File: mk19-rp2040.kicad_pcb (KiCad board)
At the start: 2 copper layers, 130 x 102 mm, 145 parts, among them J1 USB_C_Receptacle_USB2.0, J10 Conn_01x02, J11 Conn_01x03_Socket, J12 USB_C_Receptacle_USB2.0, J13 USB_C_Receptacle_USB2.0, J2 Conn_01x03_Socket, J3 Conn_01x02_Socket, J4 Conn_01x06_Socket, J5 Conn_01x02, J7 Conn_01x02_Socket, J8 Conn_01x02_Socket, J9 Conn_01x02_Socket, T1 Conn_01x01_Socket, T10 Conn_01x01_Socket, T11 Conn_01x01_Socket, T12 Conn_01x01_Socket, T13 Conn_01x01_Socket, T14 Conn_01x01_Socket, T15 Conn_01x01_Socket, T2 Conn_01x01_Socket, T3 Conn_01x01_Socket, T5 Conn_01x01_Socket, T6 Conn_01x01_Socket, T7 Conn_01x01_Socket, T9 Conn_01x01_Socket, U1 RP2040, U10 1N4148W_C81598, U11 1N4148W_C81598, U12 1N4148W_C81598, U13 1N4148W_C81598, U14 1N4148W_C81598, U15 1N4148W_C81598, U16 W25Q128JVSIQTR, U3 XC6210B332MR-G, U6 8_01A0_008200, U7 8_01A0_008200, U9 1N4148W_C81598, Y1 Crystal_GND24

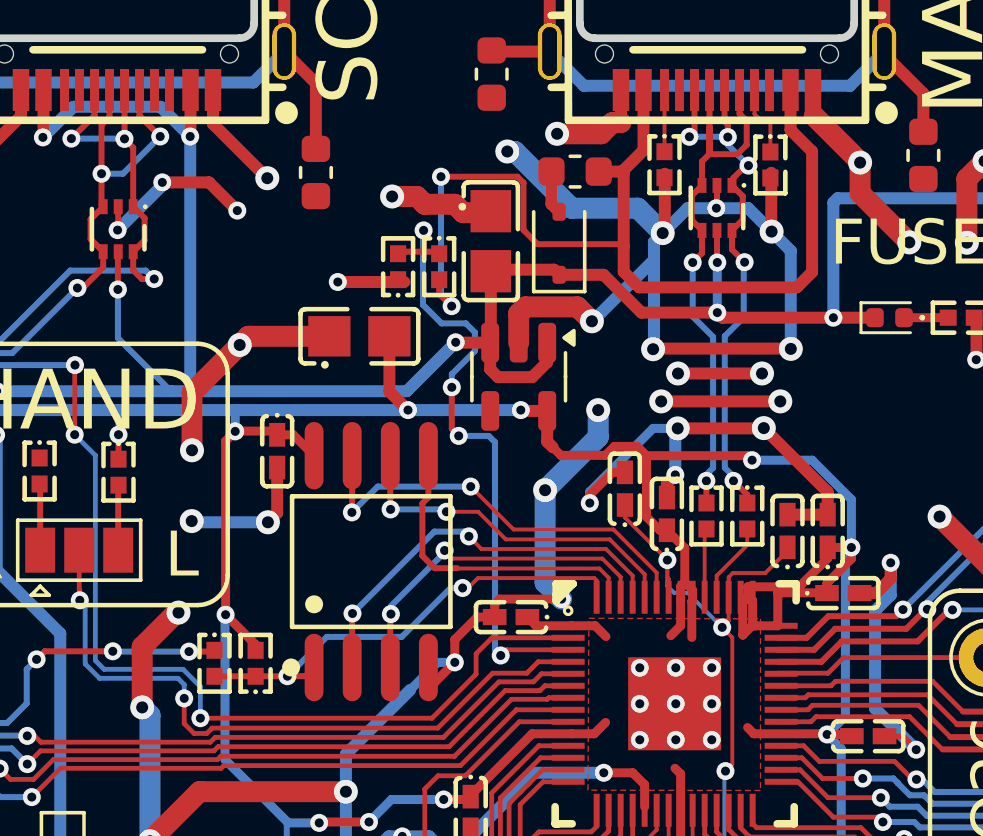
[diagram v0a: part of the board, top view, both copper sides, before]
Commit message: reworking the voltage regulator capacitors
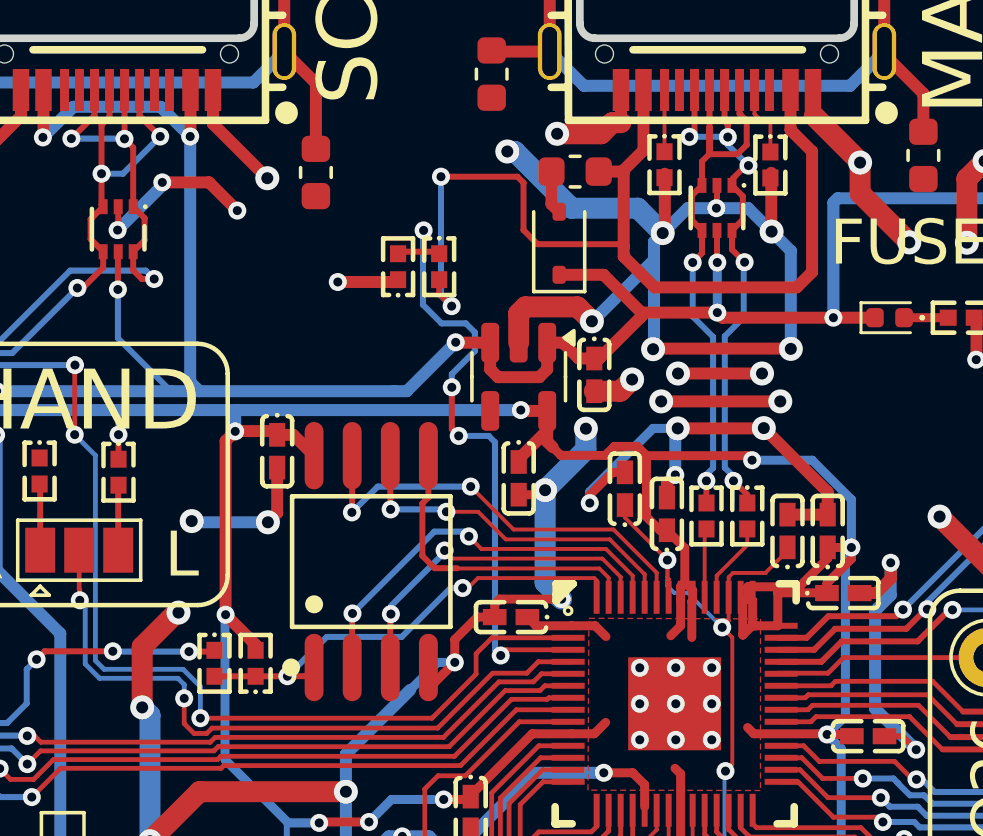
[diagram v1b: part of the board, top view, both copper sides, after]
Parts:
- C1, C27: value 10u -> 1u; footprint ct-kicad:C0805 -> ct-kicad:C0402
- moved C27 7.11 mm to (144.5, 80.3), turned to -90 degrees
- moved C1 5.63 mm to (147.0, 76.9)
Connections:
- C1 pad 1: GND -> +5V
- C1 pad 2: +5V -> GND
- C27 pad 1: GND -> +3V3
- C27 pad 2: +3V3 -> GND
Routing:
- net GND: track 776.2 -> 766.8 mm, vias 230 -> 228
- net +3V3: track 352.0 -> 351.4 mm, vias 33 -> 32
- net +5V: track 316.5 -> 316.0 mm

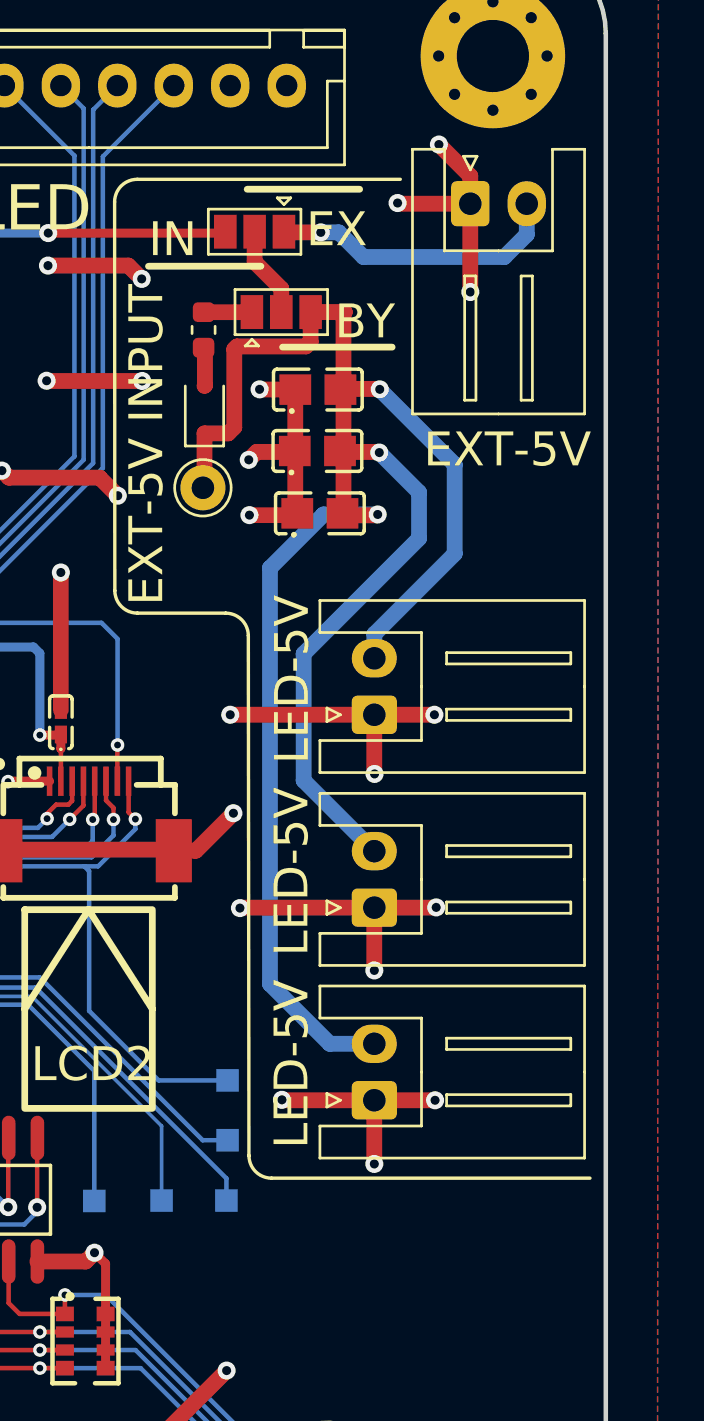
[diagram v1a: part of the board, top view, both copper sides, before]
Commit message: removing the other 10u caps and relocating the power in plug
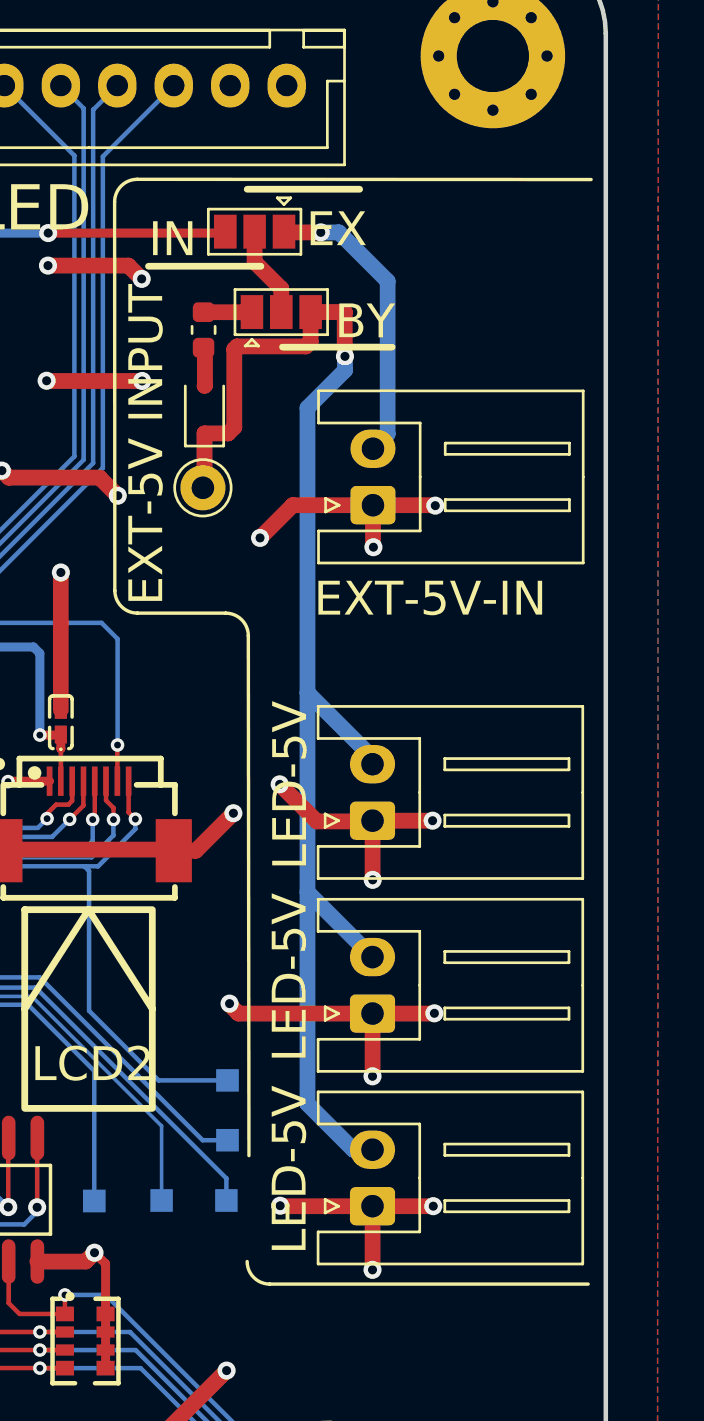
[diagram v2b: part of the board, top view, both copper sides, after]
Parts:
- removed C2, C28, C29: 10u, ct-kicad:C0805
- moved PWR-EXT-IN1 14.0 mm to (205.8, 84.2), turned to 90 degrees
- moved J7 4.69 mm to (205.8, 115.2)
- moved J8 4.69 mm to (205.8, 106.7)
- moved J9 4.69 mm to (205.8, 98.2)
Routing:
- net LED_5V: track 93.8 -> 61.6 mm, vias 3 -> 1
- net GND: track 766.8 -> 754.2 mm, vias 228 -> 225
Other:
- board text added: "EXT-5V-IN"
- board text removed: "EXT-5V"

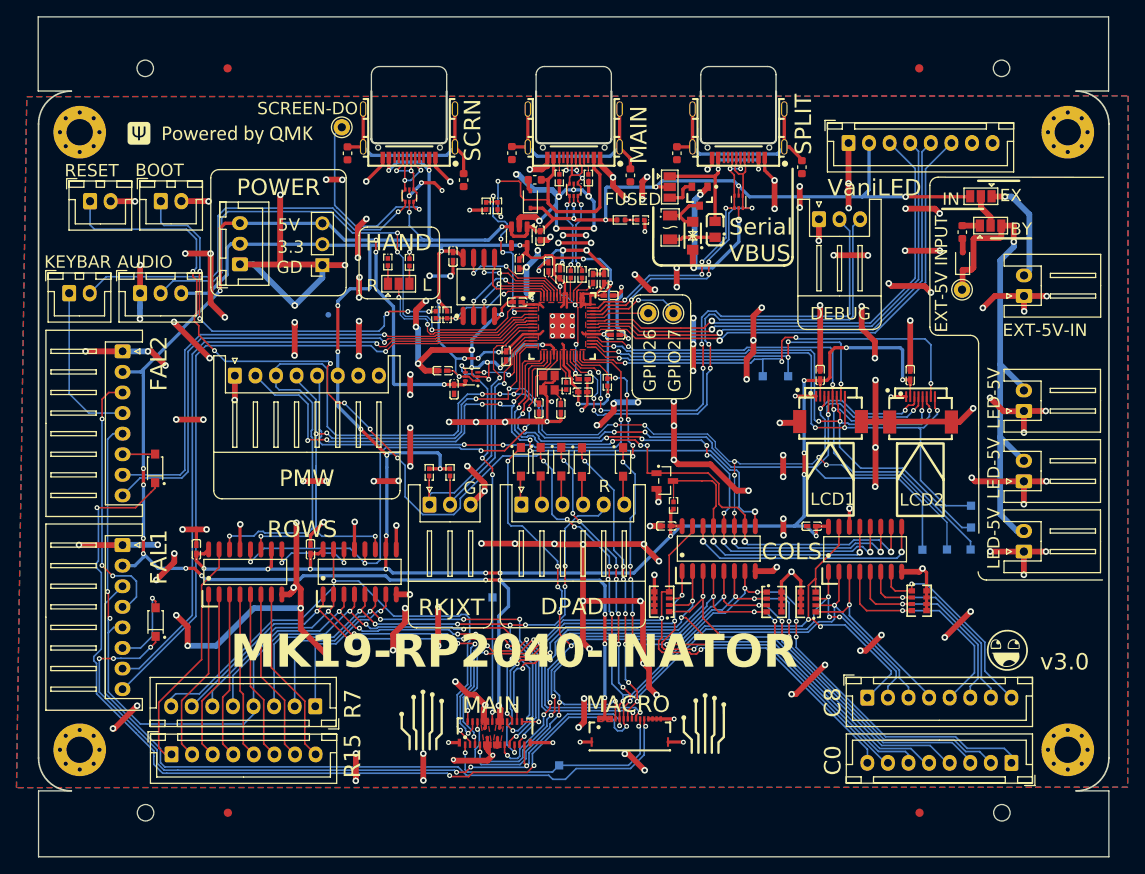
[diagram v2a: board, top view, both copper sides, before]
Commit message: replaced the macro connector with a more solid-looking part, more rework
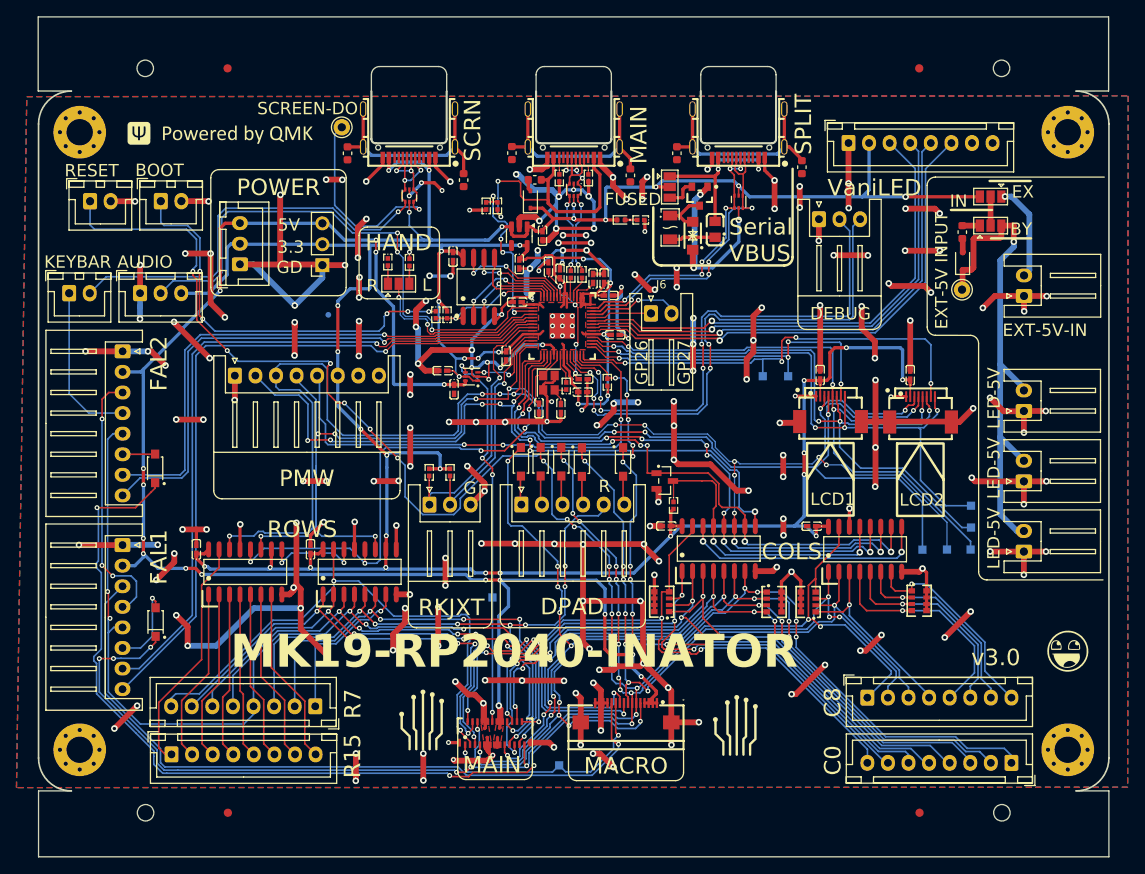
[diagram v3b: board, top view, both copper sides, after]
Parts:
- removed T5, T6: Conn_01x01_Socket, Connector_Pin:Pin_D1.0mm_L10.0mm
- added J6: Conn_01x02_Socket, Connector_JST:JST_XH_S2B-XH-A_1x02_P2.50mm_Horizontal, F.Cu at (160.5, 86.3)
- CYBOARD-MACRO1: value HC-FPC-05-10-16RLTAG -> AFC04-S16ECA-00; footprint ct-kicad:FPC-SMD_16P-P0.50_HCTL_HC-FPC-05-10-16RLTAG -> ct-kicad:FPC-SMD_AFC04-S16ECA-00
- moved LOGO1 7.34 mm to (211.2, 127.2)
- moved LOGO4 7.34 mm to (211.1, 127.3)
- moved LOGO6 3.85 mm to (170.9, 135.9)
- moved CYBOARD-MACRO1 2.21 mm to (157.4, 134.8), turned to 0 degrees
- moved JP4 1.18 mm to (201.7, 72.1)
- moved C1 0.30 mm to (147.3, 76.9)
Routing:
- net GND: track 754.2 -> 788.7 mm, vias 225 -> 231
- net col6: track 135.6 -> 140.3 mm, vias 13 -> 14
- net +5V: track 316.0 -> 319.1 mm
- net LED_FAL1_DI: track 90.4 -> 88.8 mm
- net col9: track 87.3 -> 85.7 mm
- net row3: track 84.0 -> 82.7 mm
- net Net-(JP4-A): track 13.2 -> 12.0 mm
- net Net-(J10-Pin_1): track 117.1 -> 116.0 mm
- net col8: track 202.5 -> 201.6 mm, vias 15 -> 16
- net LED_MACRO_DI: track 29.7 -> 28.9 mm
- net PMW_CS: track 60.3 -> 59.7 mm
- net SPI1_MOSI: track 170.8 -> 170.2 mm
- net Net-(JP1-C): track 4.05 -> 3.53 mm
- net +3V3: track 351.4 -> 350.9 mm
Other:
- board text added: "GP26"
- board text added: "GP27"

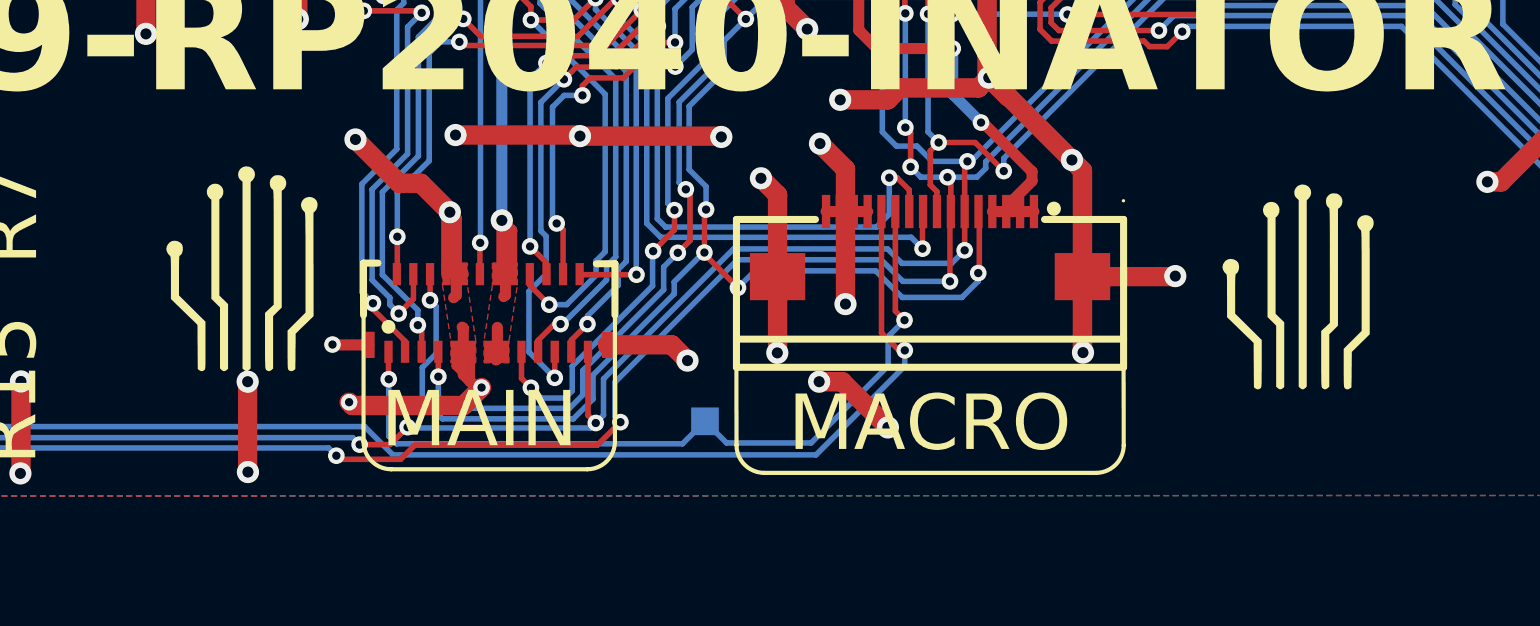
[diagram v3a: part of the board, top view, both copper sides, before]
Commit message: updating silkscreens
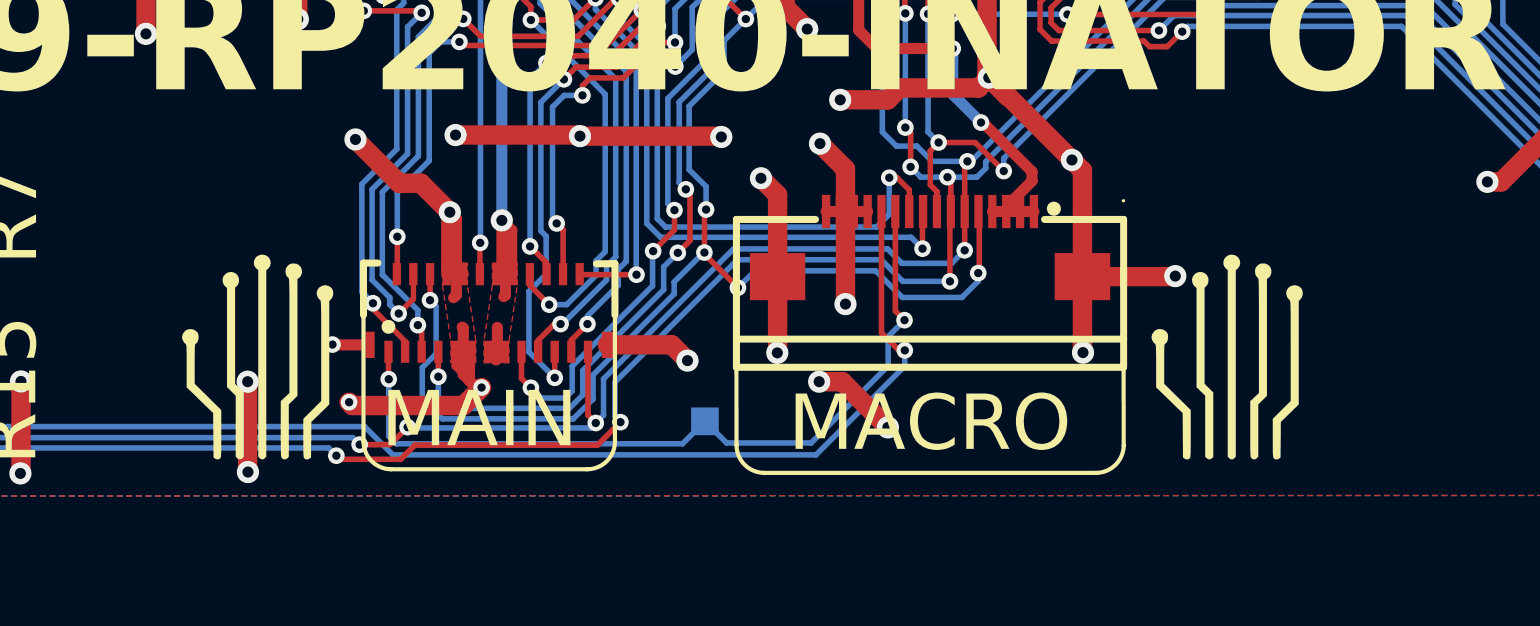
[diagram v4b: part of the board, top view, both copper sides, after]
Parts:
- moved LOGO6 3.60 mm to (168.3, 138.5)
- moved LOGO7 3.24 mm to (133.3, 138.5)
